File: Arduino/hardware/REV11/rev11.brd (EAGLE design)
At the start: 79 x 79 mm, 32 parts, among them IC2 ATMEGA168-AU, Q1 32768Hz

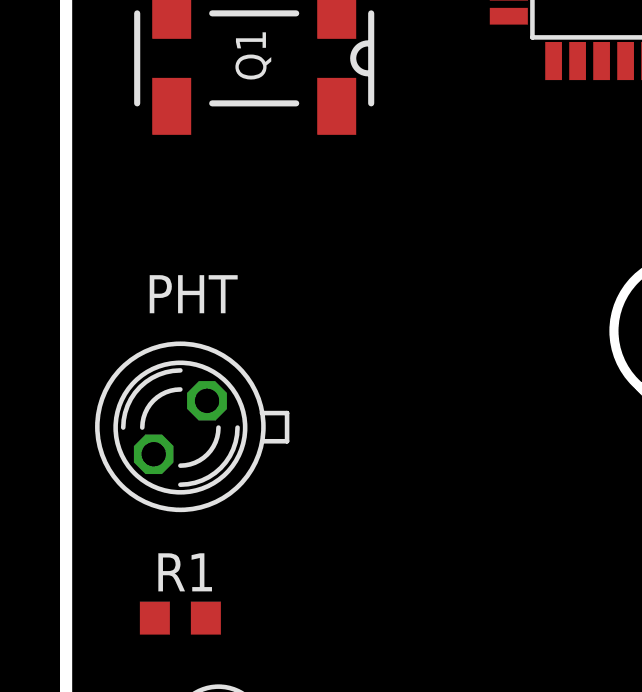
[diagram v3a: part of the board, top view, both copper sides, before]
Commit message: rotated LDR
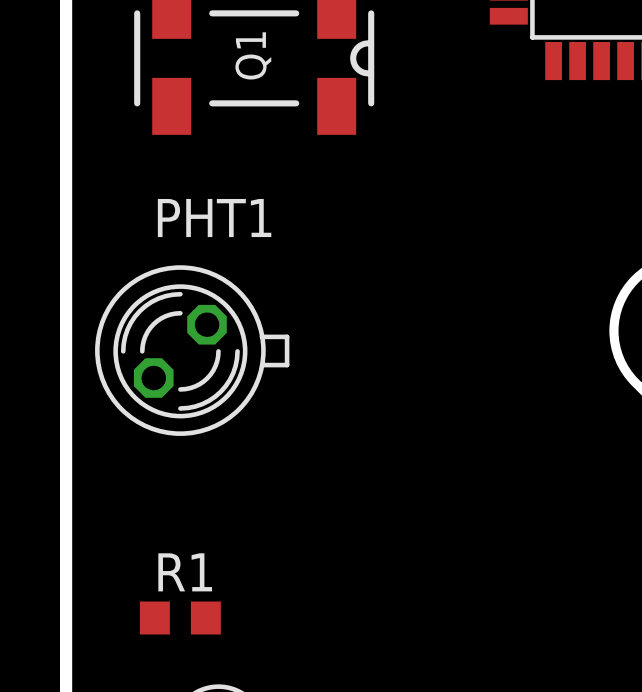
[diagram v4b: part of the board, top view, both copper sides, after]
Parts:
- removed PHT: BPX65, opto-trans-siemens:BPX65
- added PHT1: BPX65, opto-trans-siemens:BPX65
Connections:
- net IO_POWER_UP: now also PHT1.A; no longer PHT.K
- net LDR: now also PHT1.K; no longer PHT.A
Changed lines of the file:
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@@
 <attribute name="NAME" x="2.921" y="17.399" size="1.27" layer="25"/>
-</element>
-<element name="PHT" library="opto-trans-siemens" package="BPX65" value="BPX65" x="3.81" y="22.86" smashed="yes" rot="R180">
-<attribute name="OC_NEWARK" value="06WX2764" x="3.81" y="29.21" size="1.778" layer="27" rot="R180" display="off"/>
-<attribute name="OC_FARNELL" value="327451" x="3.81" y="29.21" size="1.778" layer="27" rot="R180" display="off"/>
-<attribute name="MF" value="" x="3.81" y="29.21" size="1.778" layer="27" rot="R180" display="off"/>
-<attribute name="MPN" value="BPX65." x="3.81" y="29.21" size="1.778" layer="27" rot="R180" display="off"/>
-<attribute name="NAME" x="5.715" y="27.94" size="1.27" layer="25" ratio="10" rot="R180"/>
 </element>
 <element name="R3" library="resistor" package="0309V" value="" x="3.81" y="12.7" rot="R180"/>
@@
 <attribute name="NAME" x="41.3512" y="8.9662" size="1.27" layer="25" ratio="10" rot="R180"/>
 <attribute name="VALUE" x="52.07" y="8.89" size="1.27" layer="27" rot="R180"/>
+</element>
+<element name="PHT1" library="opto-trans-siemens" package="BPX65" value="BPX65" x="3.81" y="25.4" smashed="yes" rot="R180">
+<attribute name="OC_FARNELL" value="327451" x="3.81" y="25.4" size="1.778" layer="27" rot="R180" display="off"/>
+<attribute name="MPN" value="BPX65." x="3.81" y="25.4" size="1.778" layer="27" rot="R180" display="off"/>
+<attribute name="MF" value="" x="3.81" y="25.4" size="1.778" layer="27" rot="R180" display="off"/>
+<attribute name="OC_NEWARK" value="06WX2764" x="3.81" y="25.4" size="1.778" layer="27" rot="R180" display="off"/>
+<attribute name="NAME" x="6.985" y="30.48" size="1.27" layer="25" ratio="10" rot="R180"/>
 </element>
 </elements>
@@
 <signal name="LDR">
 <contactref element="R1" pad="1"/>
-<contactref element="PHT" pad="A"/>
 <contactref element="R3" pad="2"/>
 <contactref element="IC2" pad="23"/>
-<wire x1="4.699" y1="23.749" x2="23.3426" y2="41.37" width="0" layer="19" extent="1-1"/>
-<wire x1="2.96" y1="16.51" x2="4.699" y2="23.749" width="0" layer="19" extent="1-1"/>
+<contactref element="PHT1" pad="K"/>
+<wire x1="2.96" y1="16.51" x2="23.3426" y2="41.37" width="0" layer="19" extent="1-1"/>
 <wire x1="2.54" y1="12.7" x2="2.96" y2="16.51" width="0" layer="19" extent="1-1"/>
+<wire x1="2.921" y1="24.511" x2="2.54" y2="12.7" width="0" layer="19" extent="1-1"/>
 </signal>
 <signal name="IO_POWER_UP" class="1">
-<contactref element="PHT" pad="K"/>
 <contactref element="IC2" pad="12"/>
-<wire x1="2.921" y1="21.971" x2="18.65" y2="35.0774" width="0" layer="19" extent="1-1"/>
+<contactref element="PHT1" pad="A"/>
+<wire x1="4.699" y1="26.289" x2="18.65" y2="35.0774" width="0" layer="19" extent="1-1"/>
 </signal>
 </signals>

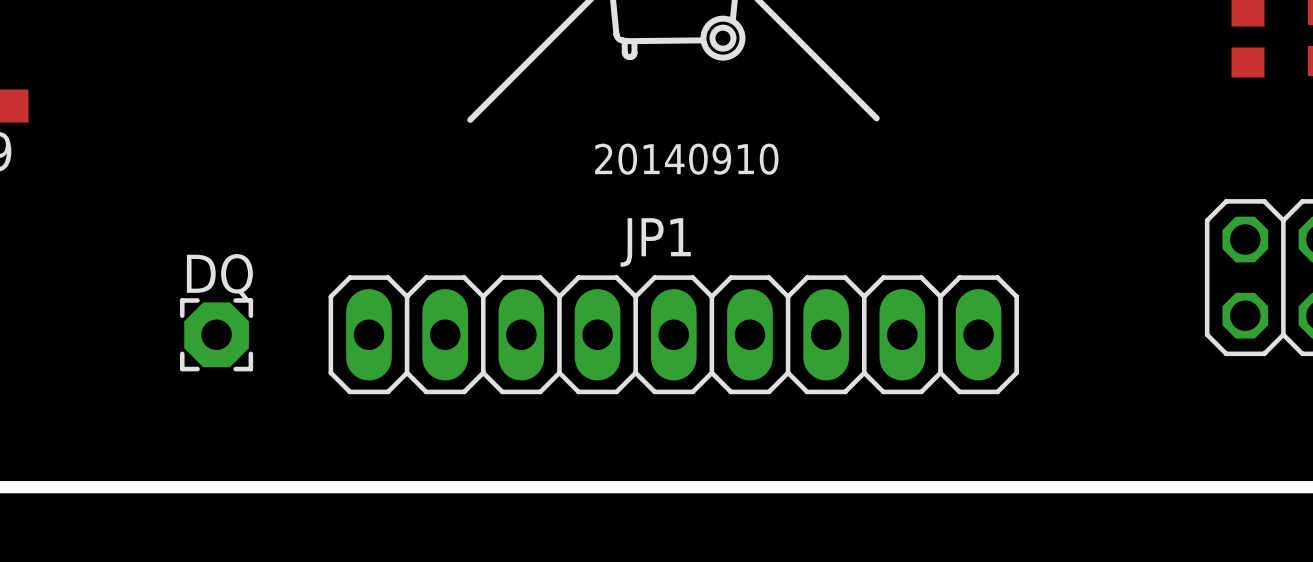
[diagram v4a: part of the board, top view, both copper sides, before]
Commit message: moved DQ/D2 to gpio connector and I2C ext
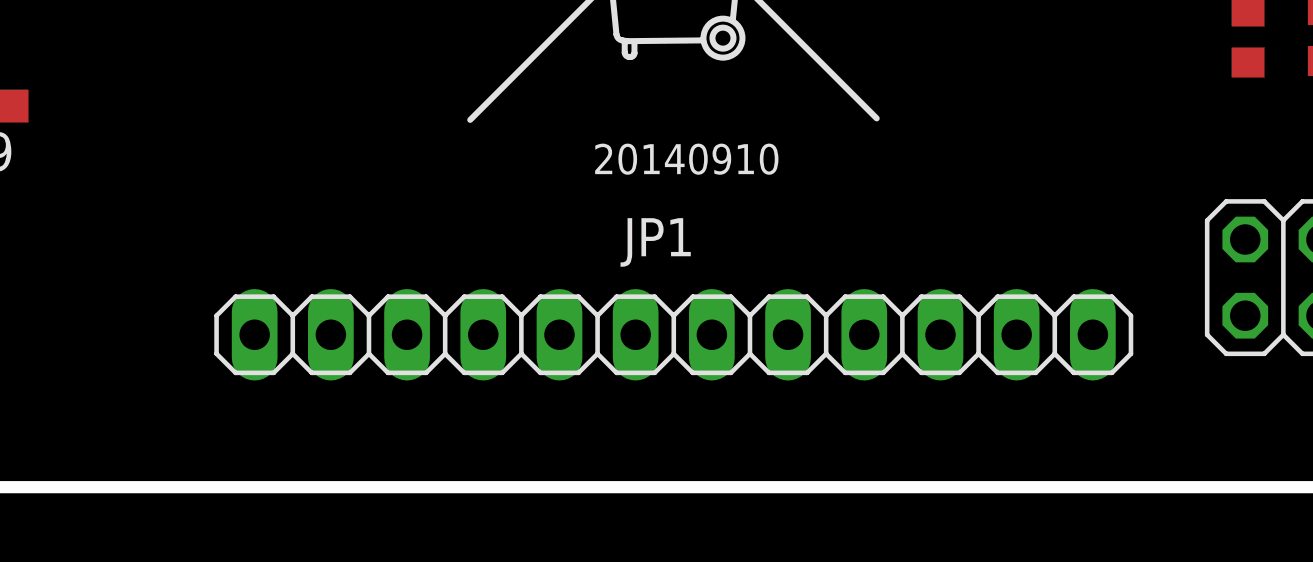
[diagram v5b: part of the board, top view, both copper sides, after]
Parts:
- removed DQ: (no value), wirepad:2,15/1,0
- JP1: device pinhead:1X09 -> pinhead:1X12
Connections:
- net D2: now also JP1.10; no longer DQ.1
- net GND: now also JP1.12
- net VCC: now also JP1.11
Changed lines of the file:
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@@
 <attribute name="NAME" x="18.669" y="11.811" size="1.27" layer="25" rot="R180"/>
 </element>
-<element name="DQ" library="wirepad" package="2,15/1,0" value="" x="25.4" y="5.08"/>
-<element name="JP1" library="pinhead" package="1X09" value="" x="40.64" y="5.08" smashed="yes" rot="R180">
+<element name="JP1" library="pinhead" package="1X12" value="" x="40.64" y="5.08" smashed="yes" rot="R180">
 <attribute name="NAME" x="41.3512" y="8.9662" size="1.27" layer="25" ratio="10" rot="R180"/>
 <attribute name="VALUE" x="52.07" y="8.89" size="1.27" layer="27" rot="R180"/>
@@
 <contactref element="I2C_EXT" pad="2"/>
 <contactref element="R9" pad="2"/>
+<contactref element="JP1" pad="11"/>
 <wire x1="70.879840625" y1="52.9883" x2="73.07053125" y2="52.97946875" width="0" layer="19" extent="1-1"/>
 <wire x1="68.03278125" y1="52.459175" x2="70.879840625" y2="52.9883" width="0" layer="19" extent="1-1"/>
@@
 <wire x1="2.05" y1="51.705" x2="15.24" y2="46.775" width="0" layer="19" extent="1-1"/>
 <wire x1="2.54" y1="76.2" x2="2.05" y2="51.705" width="0" layer="19" extent="1-1"/>
-<wire x1="2.7" y1="4" x2="10.103065625" y2="39.436453125" width="0" layer="19" extent="1-1"/>
-<wire x1="16.93" y1="12.7" x2="2.7" y2="4" width="0" layer="19" extent="1-1"/>
+<wire x1="16.93" y1="12.7" x2="23.3426" y2="37.37" width="0" layer="19" extent="1-1"/>
+<wire x1="29.21" y1="5.08" x2="16.93" y2="12.7" width="0" layer="19" extent="1-1"/>
+<wire x1="2.7" y1="4" x2="16.93" y2="12.7" width="0" layer="19" extent="1-1"/>
 <wire x1="74.93" y1="5.715" x2="69.12" y2="48.54" width="0" layer="19" extent="1-1"/>
 </signal>
@@
 <contactref element="R1" pad="2"/>
 <contactref element="R3" pad="1"/>
+<contactref element="JP1" pad="12"/>
 <wire x1="70.879840625" y1="54.6883" x2="73.07053125" y2="54.67946875" width="0" layer="19" extent="1-1"/>
 <wire x1="68.03278125" y1="55.259175" x2="70.879840625" y2="54.6883" width="0" layer="19" extent="1-1"/>
@@
 <wire x1="14.7574" y1="40.57" x2="14.7574" y2="38.97" width="0" layer="19" extent="1-1"/>
 <wire x1="11.803065625" y1="39.436453125" x2="14.7574" y2="38.97" width="0" layer="19" extent="1-1"/>
+<wire x1="4.66" y1="16.51" x2="11.803065625" y2="39.436453125" width="0" layer="19" extent="1-1"/>
+<wire x1="5.08" y1="12.7" x2="4.66" y2="16.51" width="0" layer="19" extent="1-1"/>
+<wire x1="5.3" y1="4" x2="5.08" y2="12.7" width="0" layer="19" extent="1-1"/>
+<wire x1="4" y1="4" x2="5.3" y2="4" width="0" layer="19" extent="1-1"/>
+<wire x1="26.67" y1="5.08" x2="5.3" y2="4" width="0" layer="19" extent="1-1"/>
 <wire x1="2.54" y1="72.39" x2="14.7574" y2="40.57" width="0" layer="19" extent="1-1"/>
-<wire x1="5.3" y1="4" x2="11.803065625" y2="39.436453125" width="0" layer="19" extent="1-1"/>
-<wire x1="4" y1="4" x2="5.3" y2="4" width="0" layer="19" extent="1-1"/>
-<wire x1="4.66" y1="16.51" x2="4" y2="4" width="0" layer="19" extent="1-1"/>
-<wire x1="5.08" y1="12.7" x2="4.66" y2="16.51" width="0" layer="19" extent="1-1"/>
 </signal>
 <signal name="D6">
 <contactref element="IC2" pad="10"/>
 <contactref element="JP1" pad="8"/>
-<wire x1="33.02" y1="5.08" x2="17.05" y2="35.0774" width="0" layer="19" extent="1-1"/>
+<wire x1="36.83" y1="5.08" x2="17.05" y2="35.0774" width="0" layer="19" extent="1-1"/>
 </signal>
 <signal name="SPI_SCK">
@@
 <contactref element="IC2" pad="25"/>
 <contactref element="JP1" pad="2"/>
-<wire x1="48.26" y1="5.08" x2="21.85" y2="43.6626" width="0" layer="19" extent="1-1"/>
+<wire x1="52.07" y1="5.08" x2="21.85" y2="43.6626" width="0" layer="19" extent="1-1"/>
 </signal>
 <signal name="D5">
 <contactref element="IC2" pad="9"/>
 <contactref element="JP1" pad="7"/>
-<wire x1="35.56" y1="5.08" x2="16.25" y2="35.0774" width="0" layer="19" extent="1-1"/>
+<wire x1="39.37" y1="5.08" x2="16.25" y2="35.0774" width="0" layer="19" extent="1-1"/>
 </signal>
 <signal name="D2">
 <contactref element="IC2" pad="32"/>
 <contactref element="R9" pad="1"/>
-<contactref element="DQ" pad="1"/>
+<contactref element="JP1" pad="10"/>
 <wire x1="18.63" y1="12.7" x2="16.25" y2="43.6626" width="0" layer="19" extent="1-1"/>
-<wire x1="25.4" y1="5.08" x2="18.63" y2="12.7" width="0" layer="19" extent="1-1"/>
+<wire x1="31.75" y1="5.08" x2="18.63" y2="12.7" width="0" layer="19" extent="1-1"/>
 </signal>
 <signal name="D7">
 <contactref element="IC2" pad="11"/>
 <contactref element="JP1" pad="9"/>
-<wire x1="30.48" y1="5.08" x2="17.85" y2="35.0774" width="0" layer="19" extent="1-1"/>
+<wire x1="34.29" y1="5.08" x2="17.85" y2="35.0774" width="0" layer="19" extent="1-1"/>
 </signal>
 <signal name="A1">
 <contactref element="IC2" pad="24"/>
 <contactref element="JP1" pad="1"/>
-<wire x1="50.8" y1="5.08" x2="23.3426" y2="42.17" width="0" layer="19" extent="1-1"/>
+<wire x1="54.61" y1="5.08" x2="23.3426" y2="42.17" width="0" layer="19" extent="1-1"/>
 </signal>
 <signal name="D3">
 <contactref element="IC2" pad="1"/>
 <contactref element="JP1" pad="6"/>
-<wire x1="38.1" y1="5.08" x2="14.7574" y2="42.17" width="0" layer="19" extent="1-1"/>
+<wire x1="41.91" y1="5.08" x2="14.7574" y2="42.17" width="0" layer="19" extent="1-1"/>
 </signal>
 <signal name="A3">
 <contactref element="IC2" pad="26"/>
 <contactref element="JP1" pad="3"/>
-<wire x1="45.72" y1="5.08" x2="21.05" y2="43.6626" width="0" layer="19" extent="1-1"/>
+<wire x1="49.53" y1="5.08" x2="21.05" y2="43.6626" width="0" layer="19" extent="1-1"/>
 </signal>
 <signal name="A6">
 <contactref element="IC2" pad="19"/>
 <contactref element="JP1" pad="4"/>
-<wire x1="43.18" y1="5.08" x2="23.3426" y2="38.17" width="0" layer="19" extent="1-1"/>
+<wire x1="46.99" y1="5.08" x2="23.3426" y2="38.17" width="0" layer="19" extent="1-1"/>
 </signal>
 <signal name="A7">
 <contactref element="IC2" pad="22"/>
 <contactref element="JP1" pad="5"/>
-<wire x1="40.64" y1="5.08" x2="23.3426" y2="40.57" width="0" layer="19" extent="1-1"/>
+<wire x1="44.45" y1="5.08" x2="23.3426" y2="40.57" width="0" layer="19" extent="1-1"/>
 </signal>
 <signal name="LED_HEATCALL_L">

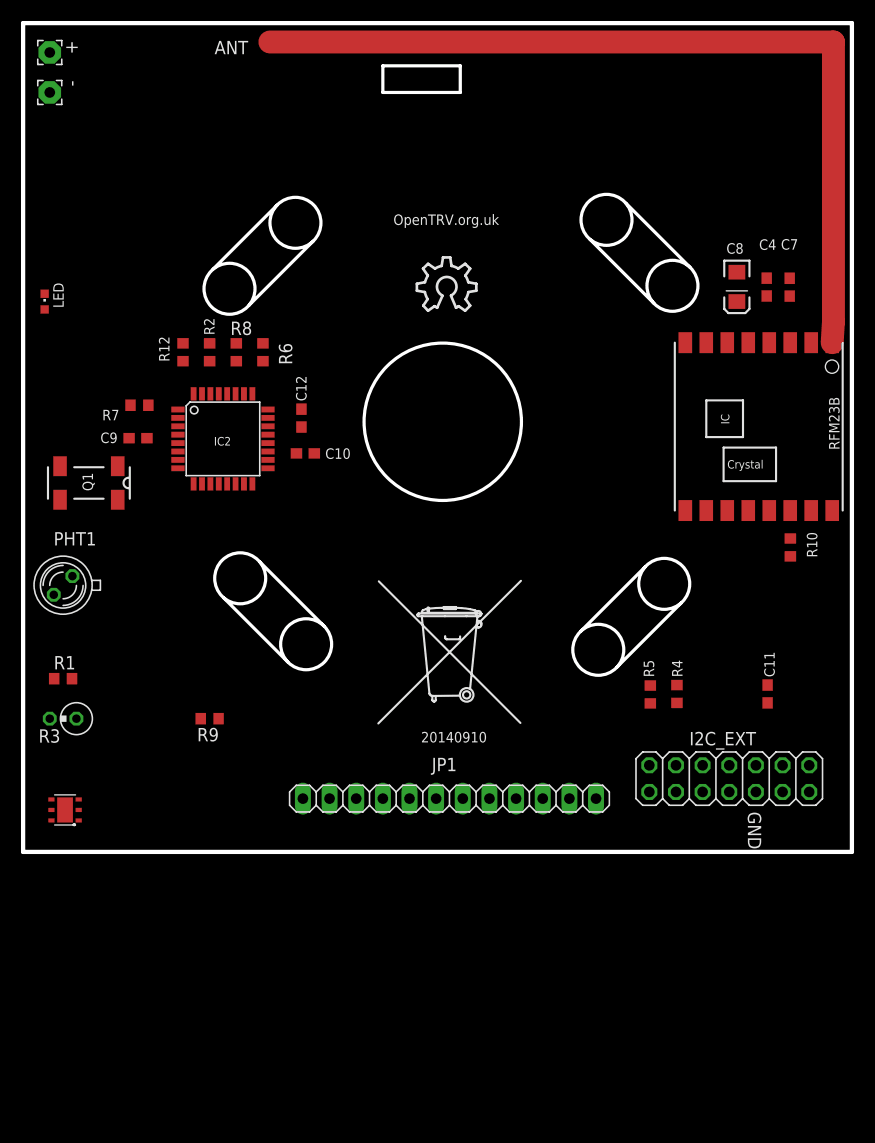
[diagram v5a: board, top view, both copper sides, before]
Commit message: corrected antenna and added copyright
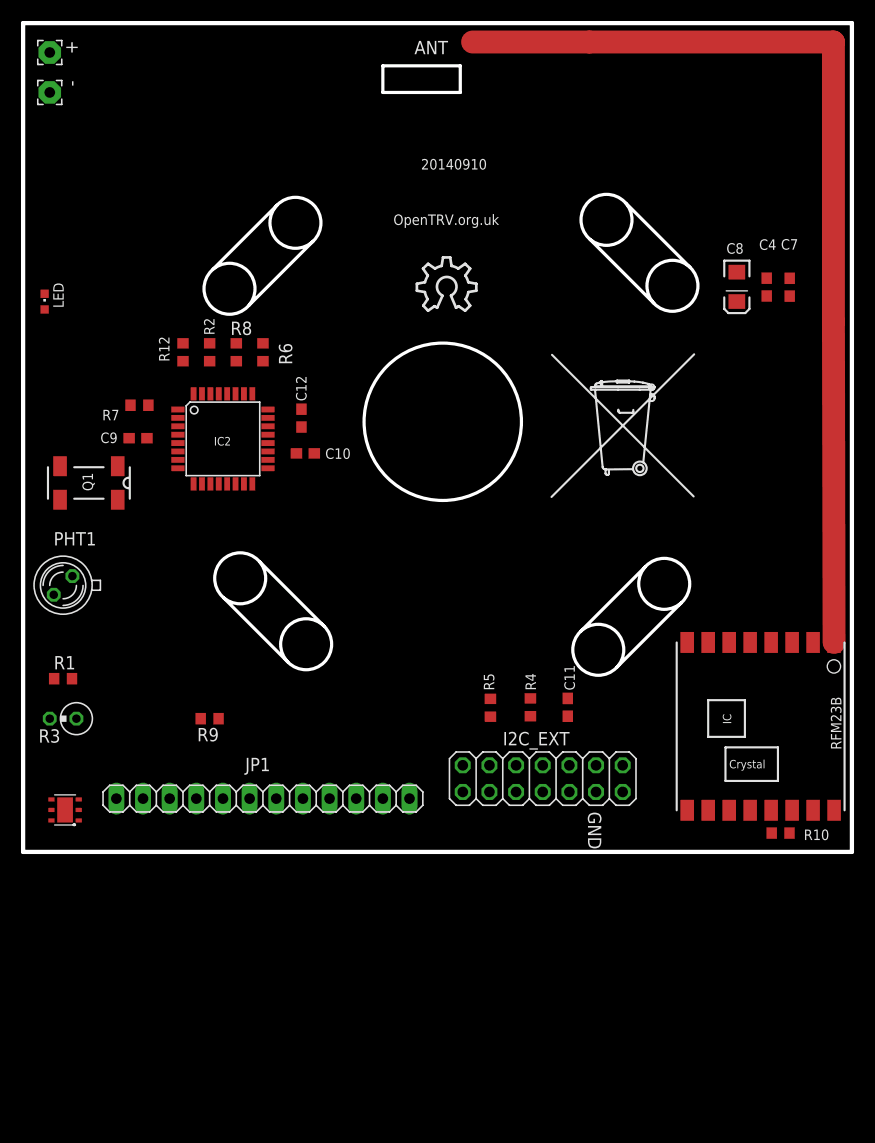
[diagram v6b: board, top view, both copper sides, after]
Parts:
- moved RFM23B 28.6 mm to (70.3, 12.0)
- moved R10 27.2 mm to (72.2, 1.79), turned to 0 degrees
- moved U$2 27.2 mm to (57.0, 37.9)
- moved C11 19.1 mm to (51.9, 13.8)
- moved ANT 19.0 mm to (43.8, 76.8)
- moved I2C_EXT 17.8 mm to (49.5, 6.99)
- moved JP1 17.8 mm to (22.9, 5.08)
- moved R5 15.3 mm to (44.5, 13.7)
- moved R4 14.0 mm to (48.4, 13.8)
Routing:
- net N$31: track 84.0 -> 101.8 mm

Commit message: rotated RFM
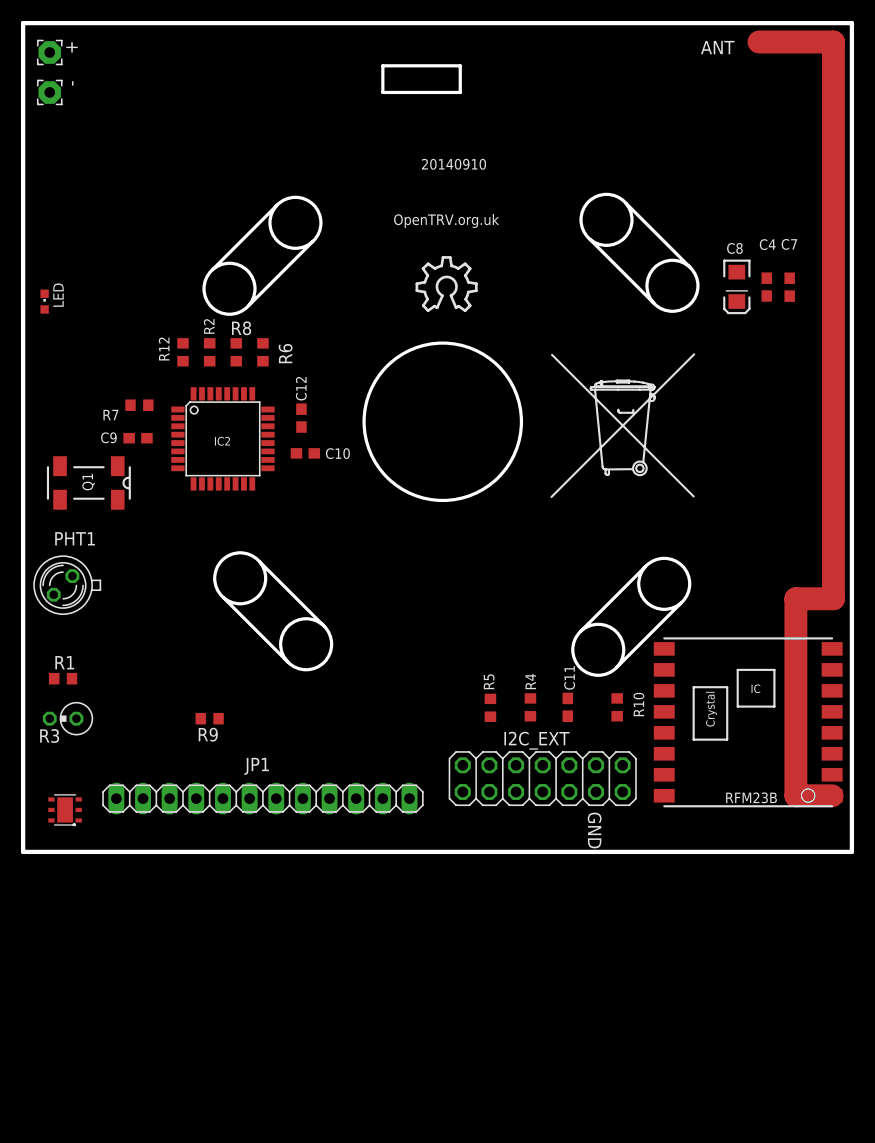
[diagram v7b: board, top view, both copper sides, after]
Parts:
- moved ANT 27.3 mm to (71.1, 76.8)
- moved R10 19.7 mm to (56.6, 13.8), turned to 90 degrees
- moved RFM23B 1.25 mm to (69.1, 12.3), turned to 180 degrees
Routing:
- net N$31: track 101.8 -> 86.0 mm

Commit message: moved rfm further down
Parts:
- moved JP1 63.6 mm to (25.4, 68.6)
- moved C8 34.4 mm to (65.5, 19.6)
- moved C4 34.3 mm to (69.6, 19.5)
- moved C7 34.3 mm to (73.1, 19.5)
- moved R4 10.2 mm to (38.2, 13.8)
- moved I2C_EXT 8.89 mm to (40.6, 6.99)
- moved R10 8.89 mm to (47.7, 13.8)
- moved R5 8.89 mm to (35.7, 13.7)
- moved C11 8.89 mm to (43.0, 13.8)
- moved RFM23B 5.39 mm to (65.3, 8.54)
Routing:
- net N$31: track 86.0 -> 86.7 mm
